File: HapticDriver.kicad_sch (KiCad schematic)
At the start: 18 parts, among them J14 USB_C_Receptacle_USB2.0, J3 BATT PWR, SW1 BOOT, SW2 EN, U1 ESP32-S3-WROOM-2, U11 REG1117-3.3, U3 74HCT595, U4 74HCT595, U5 74HCT595

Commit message: feat: major redesign with better driver and audio, partial routing
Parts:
- removed C13, C15: 10uF, Capacitor_SMD:C_1206_3216Metric_Pad1.33x1.80mm_HandSolder, symbol Device:C
- removed R1: 5K1, Resistor_SMD:R_1206_3216Metric, symbol Device:R
- removed U11: REG1117-3.3, DCY4, symbol Regulator_Ti:REG1117-3.3
- removed U3, U4, U5: 74HCT595, Package_SO:SOIC-16_3.9x9.9mm_P1.27mm, symbol 74xx:74HCT595
- C14: footprint Capacitor_SMD:C_1206_3216Metric_Pad1.33x1.80mm_HandSolder -> Capacitor_SMD:C_0603_1608Metric
- R14, R15, R16: footprint Resistor_SMD:R_1206_3216Metric -> Resistor_SMD:R_0603_1608Metric
- U1: footprint PCM_Espressif:ESP32-S3-WROOM-2 -> RF_Module:ESP32-S3-WROOM-1; Part (none) -> C2913202
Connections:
- net nFAULT_3 is gone; now on net I2S_BCLK: U1.20 (GPIO12/TOUCH12/ADC2_CH1/FSPICLK/FSPIIO6/SUBSPICLK)
- net I2S_BCLK: no longer U1.6 (GPIO6/TOUCH6/ADC1_CH5)
- net nFAULT_1: now also U1.12 (GPIO8/TOUCH8/ADC1_CH7/SUBSPICS1); no longer U1.15 (GPIO3/TOUCH3/ADC1_CH2)
- net nFAULT_2: now also U1.11 (GPIO18/U1RXD/ADC2_CH7/CLK_OUT3); no longer U1.18 (GPIO10/TOUCH10/ADC1_CH9/FSPICS0/FSPIIO4/SUBSPICS0)
- net DRV_MISO: now reaches U1.10 (GPIO17/U1TXD/ADC2_CH6)
- net I2S_DIN: now reaches U1.19 (GPIO11/TOUCH11/ADC2_CH0/FSPID/FSPIIO5/SUBSPID)
- net DRV_MOSI: now reaches U1.7 (GPIO7/TOUCH7/ADC1_CH6)
- net I2S_DATA renamed DRV_SCK
- net I2S_WS renamed DRV_CS_2
- net nFAULT_4 renamed DRV_CS_1
- net nFAULT_5 renamed I2S_WCLK
- net nFAULT_6: no longer names the net of U1.16 (GPIO46)
- no-connect marks 21 -> 16
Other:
- removed sheet Driver 3
- removed sheet Driver 4
- removed sheet Driver 5
- removed sheet Driver 6
- added sheet Audio (audio.kicad_sch)
- added sheet Power (power_reg.kicad_sch)
- sheet Driver 1 ports: added SCK, SIN, SOUT, nCS, nSLEEP; removed IN1, IN2, IN3, IN4, SCL, SDA
- sheet Driver 2 ports: added SCK, SIN, SOUT, nCS, nSLEEP; removed IN1, IN2, IN3, IN4, SCL, SDA
- note removed: "Shift Registers"

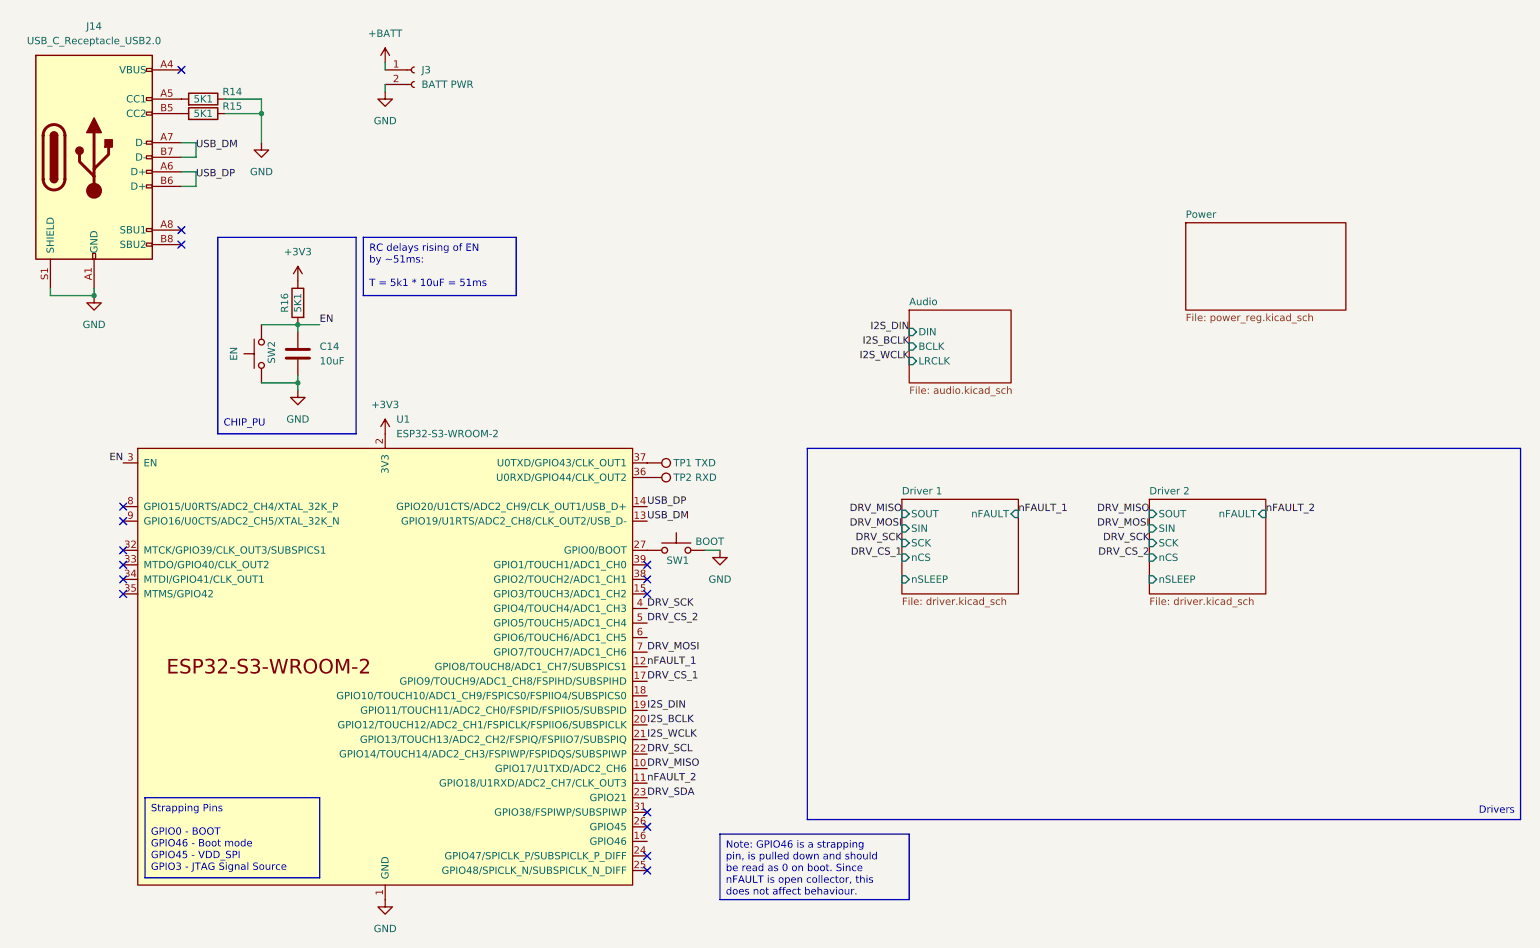
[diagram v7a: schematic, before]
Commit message: feat: full reroute with max22200 driver
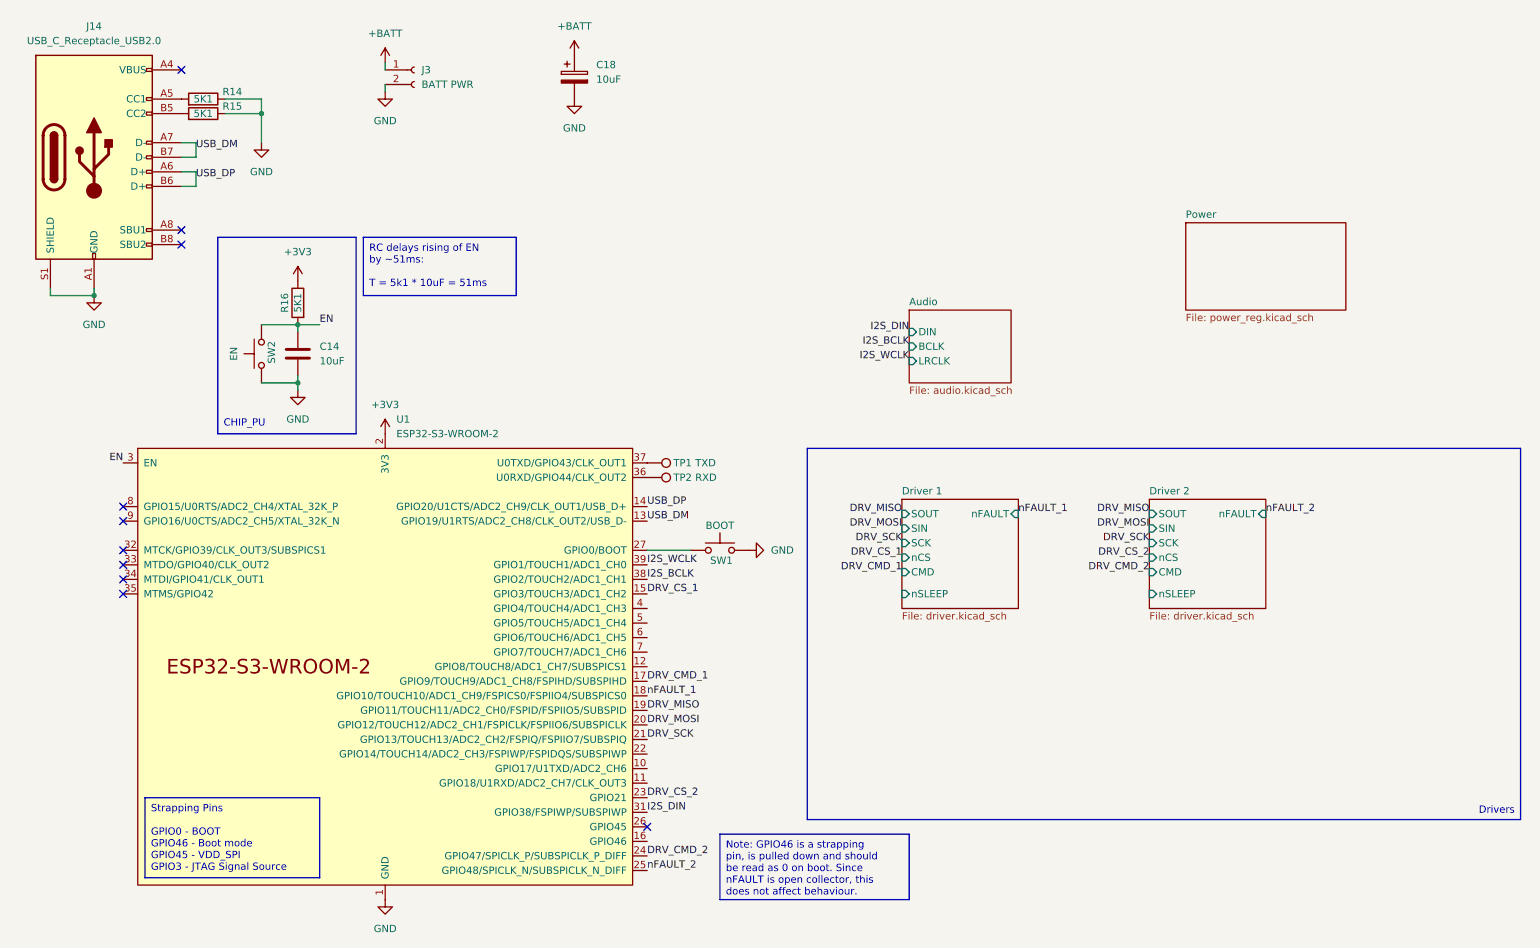
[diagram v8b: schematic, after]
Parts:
- added C18: 10uF, Capacitor_SMD:CP_Elec_4x5.4, symbol Device:C_Polarized
- J14: footprint Connector_USB:USB_C_Receptacle_GCT_USB4085 -> Connector_USB:USB_C_Receptacle_G-Switch_GT-USB-7010ASV; symbol Connector:USB_C_Receptacle_USB2.0 -> Connector:USB_C_Receptacle_USB2.0_16P
- J3: footprint Connector_Wire:SolderWire-1.5sqmm_1x02_P6mm_D1.7mm_OD3mm -> Connector_Wire:SolderWire-1sqmm_1x02_P5.4mm_D1.4mm_OD2.7mm
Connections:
- net DRV_SDA is gone; now on net DRV_CS_2: U1.23 (GPIO21)
- net +BATT: now also C18.1
- net DRV_CS_1: now also U1.15 (GPIO3/TOUCH3/ADC1_CH2); no longer U1.17 (GPIO9/TOUCH9/ADC1_CH8/FSPIHD/SUBSPIHD)
- net DRV_CS_2: no longer U1.5 (GPIO5/TOUCH5/ADC1_CH4)
- net DRV_MISO: now also U1.19 (GPIO11/TOUCH11/ADC2_CH0/FSPID/FSPIIO5/SUBSPID); no longer U1.10 (GPIO17/U1TXD/ADC2_CH6)
- net DRV_MOSI: now also U1.20 (GPIO12/TOUCH12/ADC2_CH1/FSPICLK/FSPIIO6/SUBSPICLK); no longer U1.7 (GPIO7/TOUCH7/ADC1_CH6)
- net DRV_SCK: now also U1.21 (GPIO13/TOUCH13/ADC2_CH2/FSPIQ/FSPIIO7/SUBSPIQ); no longer U1.4 (GPIO4/TOUCH4/ADC1_CH3)
- net GND: now also C18.2
- net I2S_BCLK: now also U1.38 (GPIO2/TOUCH2/ADC1_CH1); no longer U1.20 (GPIO12/TOUCH12/ADC2_CH1/FSPICLK/FSPIIO6/SUBSPICLK)
- net I2S_DIN: now also U1.31 (GPIO38/FSPIWP/SUBSPIWP); no longer U1.19 (GPIO11/TOUCH11/ADC2_CH0/FSPID/FSPIIO5/SUBSPID)
- net I2S_WCLK: now also U1.39 (GPIO1/TOUCH1/ADC1_CH0); no longer U1.21 (GPIO13/TOUCH13/ADC2_CH2/FSPIQ/FSPIIO7/SUBSPIQ)
- net nFAULT_1: now also U1.18 (GPIO10/TOUCH10/ADC1_CH9/FSPICS0/FSPIIO4/SUBSPICS0); no longer U1.12 (GPIO8/TOUCH8/ADC1_CH7/SUBSPICS1)
- net nFAULT_2: now also U1.25 (GPIO48/SPICLK_N/SUBSPICLK_N_DIFF); no longer U1.11 (GPIO18/U1RXD/ADC2_CH7/CLK_OUT3)
- net DRV_CMD_2: now reaches U1.24 (GPIO47/SPICLK_P/SUBSPICLK_P_DIFF)
- net DRV_SCL: no longer names the net of U1.22 (GPIO14/TOUCH14/ADC2_CH3/FSPIWP/FSPIDQS/SUBSPIWP)
- new net DRV_CMD_1: U1.17 (GPIO9/TOUCH9/ADC1_CH8/FSPIHD/SUBSPIHD)
- no-connect marks 16 -> 10
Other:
- sheet Driver 1 ports: added CMD; removed none
- sheet Driver 2 ports: added CMD; removed none
- moved on the sheet: SW1
